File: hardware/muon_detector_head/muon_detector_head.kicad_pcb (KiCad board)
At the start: 2 copper layers, 60 x 75 mm, 22 parts, among them J1 Conn_01x08, U1 TPH2502, U2 TLV3502

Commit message: accepting updates
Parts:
- moved J1 11.4 mm to (7.55, 9.85)
- moved C6 2.55 mm to (32.0, 24.4)
- renumbered REF** to H1, REF** to H2, REF** to H3, REF** to H4
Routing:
- net VBIAS: track 33.3 -> 0.00 mm, vias 1 -> 0
- net GND: track 1.09 -> 0.00 mm, vias 1 -> 0
- net /SIPM_RAW: track 1.05 -> 0.00 mm
- added copper zone on B.Cu, net GND
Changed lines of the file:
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@@
 	)
 	(setup
+		(stackup
+			(layer "F.SilkS"
+				(type "Top Silk Screen")
+				(color "White")
+			)
+			(layer "F.Paste"
+				(type "Top Solder Paste")
+			)
+			(layer "F.Mask"
+				(type "Top Solder Mask")
+				(color "Green")
+				(thickness 0.01)
+			)
+			(layer "F.Cu"
+				(type "copper")
+				(thickness 0.035)
+			)
+			(layer "dielectric 1"
+				(type "core")
+				(thickness 1.51)
+				(material "FR4")
+				(epsilon_r 4.5)
+				(loss_tangent 0.02)
+			)
+			(layer "B.Cu"
+				(type "copper")
+				(thickness 0.035)
+			)
+			(layer "B.Mask"
+				(type "Bottom Solder Mask")
+				(color "Green")
+				(thickness 0.01)
+			)
+			(layer "B.Paste"
+				(type "Bottom Solder Paste")
+			)
+			(layer "B.SilkS"
+				(type "Bottom Silk Screen")
+				(color "White")
+			)
+			(copper_finish "None")
+			(dielectric_constraints no)
+		)
 		(pad_to_mask_clearance 0)
 		(allow_soldermask_bridges_in_footprints no)
@@
 		(descr "Mounting Hole 2.5mm, no annular, generated by kicad-footprint-generator mountinghole.py")
 		(tags "mountinghole")
-		(property "Reference" "REF**"
+		(property "Reference" "H1"
 			(at 0 -3.45 0)
 			(layer "F.SilkS")
+			(hide yes)
 			(effects
 				(font
@@
 			)
 		)
-		(attr exclude_from_pos_files exclude_from_bom)
+		(attr board_only exclude_from_pos_files exclude_from_bom)
 		(fp_circle
 			(center 0 0)
@@
 		(descr "Mounting Hole 2.5mm, no annular, generated by kicad-footprint-generator mountinghole.py")
 		(tags "mountinghole")
-		(property "Reference" "REF**"
+		(property "Reference" "H2"
 			(at 0 -3.45 0)
 			(layer "F.SilkS")
+			(hide yes)
 			(effects
 				(font
@@
 			)
 		)
-		(attr exclude_from_pos_files exclude_from_bom)
+		(attr board_only exclude_from_pos_files exclude_from_bom)
 		(fp_circle
 			(center 0 0)
@@
 		(descr "Mounting Hole 2.5mm, no annular, generated by kicad-footprint-generator mountinghole.py")
 		(tags "mountinghole")
-		(property "Reference" "REF**"
+		(property "Reference" "H3"
 			(at 0 -3.45 0)
 			(layer "F.SilkS")
+			(hide yes)
 			(effects
 				(font
@@
 			)
 		)
-		(attr exclude_from_pos_files exclude_from_bom)
+		(attr board_only exclude_from_pos_files exclude_from_bom)
 		(fp_circle
 			(center 0 0)
@@
 		(descr "Mounting Hole 2.5mm, no annular, generated by kicad-footprint-generator mountinghole.py")
 		(tags "mountinghole")
-		(property "Reference" "REF**"
+		(property "Reference" "H4"
 			(at 0 -3.45 0)
 			(layer "F.SilkS")
+			(hide yes)
 			(effects
 				(font
@@
 			)
 		)
-		(attr exclude_from_pos_files exclude_from_bom)
+		(attr board_only exclude_from_pos_files exclude_from_bom)
 		(fp_circle
 			(center 0 0)
@@
 	(footprint "Connector_PinHeader_2.54mm:PinHeader_1x08_P2.54mm_Vertical"
 		(layer "B.Cu")
-		(at 11.6 20.5 180)
+		(at 7.55 9.85 180)
 		(descr "Through hole straight pin header, 1x08, 2.54mm pitch, single row")
 		(tags "Through hole pin header THT 1x08 2.54mm single row")
@@
 	(footprint "Capacitor_SMD:C_0805_2012Metric"
 		(layer "B.Cu")
-		(at 32 27 180)
+		(at 32 24.45 180)
 		(descr "Capacitor SMD 0805 (2012 Metric), square (rectangular) end terminal, IPC-7351 nominal, (Body size source: IPC-SM-782 page 76, https://www.pcb-3d.com/wordpress/wp-content/uploads/ipc-sm-782a_amendment_1_and_2.pdf, https://docs.google.com/spreadsheets/d/1BsfQQcO9C6DZCsRaXUlFlo91Tg2WpOkGARC1WS5S8t0/edit?usp=sharing), generated with kicad-footprint-generator")
 		(tags "capacitor")
@@
 	)
 	(segment
-		(start 27 27.15)
-		(end 27 28.2)
-		(width 0.5)
-		(layer "F.Cu")
-		(net 2)
-	)
-	(via
-		(at 20.4875 35)
-		(size 0.6)
-		(drill 0.3)
-		(layers "F.Cu" "B.Cu")
-		(net 3)
-	)
-	(segment
-		(start 21.575 35)
-		(end 20.4875 35)
-		(width 0.5)
-		(layer "B.Cu")
-		(net 3)
-	)
-	(segment
-		(start 33 32.85)
-		(end 34.65 32.85)
-		(width 0.5)
-		(layer "F.Cu")
-		(net 7)
-	)
-	(segment
-		(start 34.65 32.85)
-		(end 34.7 32.8)
-		(width 0.5)
-		(layer "F.Cu")
-		(net 7)
-	)
-	(via
-		(at 34.7 32.8)
-		(size 0.6)
-		(drill 0.3)
-		(layers "F.Cu" "B.Cu")
-		(net 7)
-	)
-	(segment
-		(start 34.7 32.8)
-		(end 34.7 27)
-		(width 0.5)
-		(layer "B.Cu")
-		(net 7)
-	)
-	(segment
-		(start 32.95 27)
-		(end 26.45 20.5)
-		(width 0.5)
-		(layer "B.Cu")
-		(net 7)
-	)
-	(segment
-		(start 26.45 20.5)
-		(end 11.6 20.5)
-		(width 0.5)
-		(layer "B.Cu")
-		(net 7)
-	)
-	(segment
-		(start 34.7 27)
-		(end 32.95 27)
-		(width 0.5)
-		(layer "B.Cu")
-		(net 7)
-	)
-	(segment
 		(start 40.925 48.9875)
 		(end 40.9125 49)
-		(width 0.25)
+		(width 0.5)
 		(layer "B.Cu")
 		(net 9)
@@
 		(start 25.365 43.550001)
 		(end 25.365 44.525)
-		(width 0.25)
+		(width 0.5)
 		(layer "B.Cu")
 		(net 10)
@@
 		(start 34.85 60.75)
 		(end 36 60.75)
-		(width 0.25)
+		(width 0.5)
 		(layer "B.Cu")
 		(net 13)
@@
 			)
 		)
+	)
+	(zone
+		(net 3)
+		(net_name "GND")
+		(layer "B.Cu")
+		(hatch edge 0.5)
+		(connect_pads
+			(clearance 0.4)
+		)
+		(min_thickness 0.4)
+		(filled_areas_thickness no)
+		(fill yes
+			(thermal_gap 0.4)
+			(thermal_bridge_width 0.5)
+		)
+		(polygon
+			(pts
+				(xy 1 1) (xy 59 1) (xy 59 74) (xy 1 74)
+			)
+		)

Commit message: autorouting bad
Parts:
- C1, C2, C3, C4, C5, C6, J1, R1, R2, R3, R4, R5, R6, R7, RV1, U1, U2: moved to F.Cu
- D1: moved to B.Cu
- moved J1 49.0 mm to (56.5, 11.8), turned to 0 degrees
- moved C5 48.3 mm to (49.4, 23.4), turned to -90 degrees
- moved C4 47.3 mm to (52.3, 23.4), turned to -90 degrees
- moved C3 45.0 mm to (49.0, 18.6), turned to -90 degrees
- moved C2 44.9 mm to (51.6, 18.5), turned to -90 degrees
- moved R7 40.7 mm to (52.3, 33.0), turned to 0 degrees
- moved U2 30.5 mm to (50.8, 40.3), turned to 180 degrees
- moved R5 27.4 mm to (44.4, 31.7)
- moved R6 26.4 mm to (45.2, 38.6), turned to -90 degrees
- moved R1 21.7 mm to (40.6, 23.1), turned to 90 degrees
- moved C1 18.5 mm to (39.8, 26.7), turned to 180 degrees
- moved RV1 17.3 mm to (51.1, 49.5), turned to 90 degrees
- moved U1 16.7 mm to (40.0, 37.9)
- moved C6 15.4 mm to (28.0, 39.4), turned to 0 degrees
- moved R2 12.7 mm to (39.7, 29.2)
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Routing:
- net +3.3V: track 0.00 -> 113.7 mm
- net VBIAS: track 0.00 -> 90.9 mm
- net +5V: track 0.00 -> 65.5 mm, vias 0 -> 1
- net GND: track 0.00 -> 60.1 mm, vias 0 -> 3
- net /VBASE: track 0.00 -> 41.6 mm, vias 0 -> 2
- net /VBASE_DIV: track 0.02 -> 30.8 mm
- net /AMP_OUT: track 0.00 -> 16.6 mm
- net /SIPM_RAW: track 0.00 -> 12.5 mm, vias 0 -> 1
- net Net-(R7-Pad2): track 0.00 -> 11.0 mm
- net Net-(U1A--): track 0.97 -> 10.9 mm
- net /VTH: track 1.15 -> 10.8 mm
- net /AMP_IN: track 0.05 -> 9.00 mm
- net /TRIG: track 0.00 -> 8.11 mm

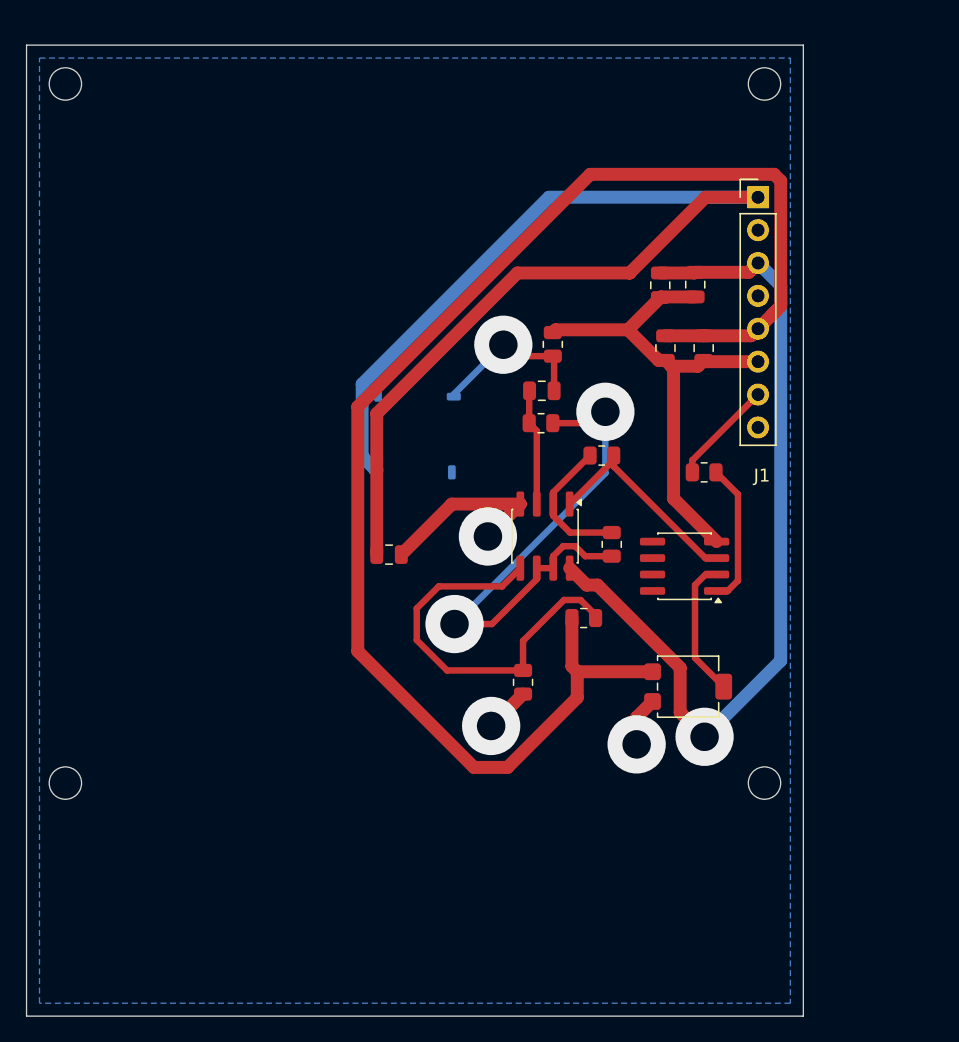
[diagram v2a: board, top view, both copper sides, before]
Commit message: feat: update detector head to include adc
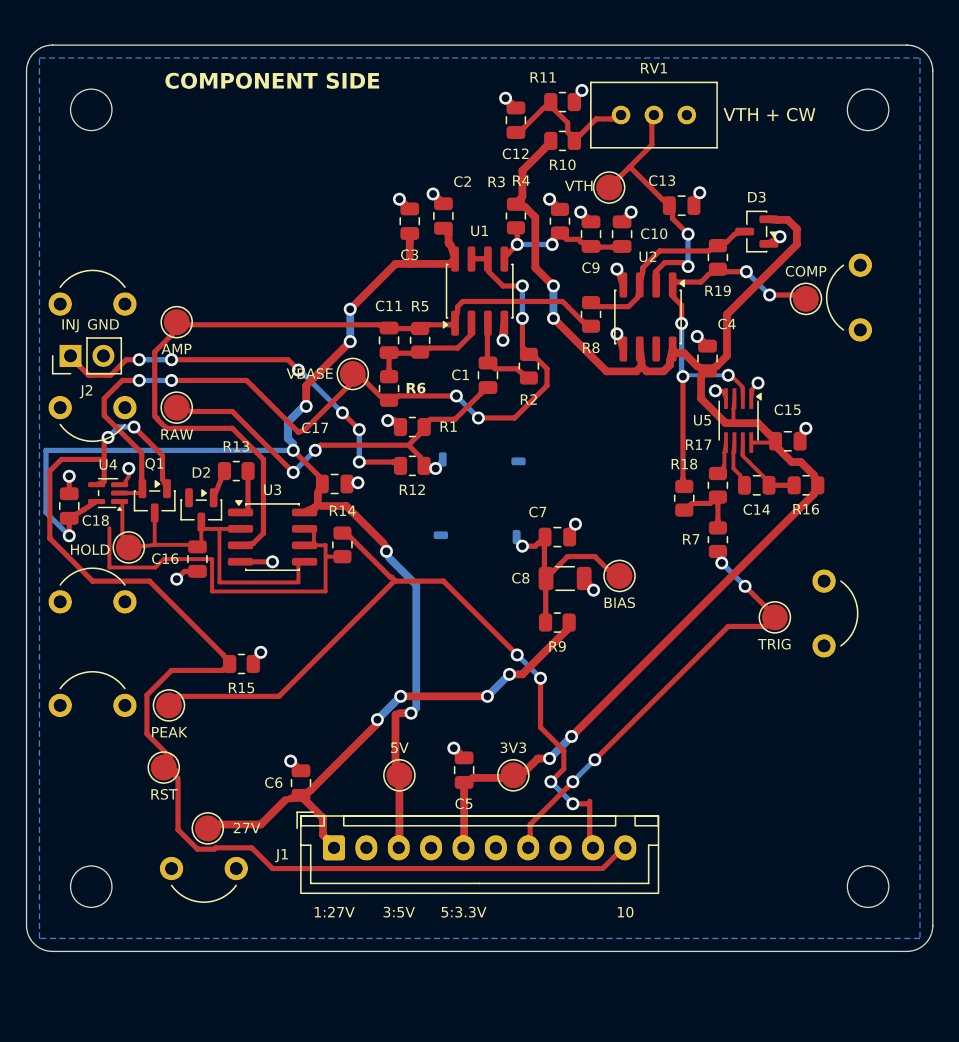
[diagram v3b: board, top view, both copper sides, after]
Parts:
- added C10: 100n, Capacitor_SMD:C_0805_2012Metric, F.Cu at (46.0, 14.6)
- added C11: 2.2p C0G, Capacitor_SMD:C_0805_2012Metric, F.Cu at (28.0, 22.8)
- added C12: 1u, Capacitor_SMD:C_0805_2012Metric, F.Cu at (37.8, 5.80)
- added C13: 10n 100V C0G, Capacitor_SMD:C_0805_2012Metric, F.Cu at (50.6, 12.4)
- added C14: 27p C0G, Capacitor_SMD:C_0805_2012Metric, F.Cu at (56.4, 34.0)
- added C15: 100n, Capacitor_SMD:C_0805_2012Metric, F.Cu at (58.8, 30.6)
- added C16: 220p C0G, Capacitor_SMD:C_0805_2012Metric, F.Cu at (13.2, 39.7)
- added C17: 100n, Capacitor_SMD:C_0805_2012Metric, F.Cu at (23.8, 33.9)
- added C18: 100n, Capacitor_SMD:C_0805_2012Metric, F.Cu at (3.30, 35.6)
- added C7: 10n 100V C0G, Capacitor_SMD:C_0805_2012Metric, F.Cu at (41.0, 38.0)
- added C8: 1u 50V, Capacitor_SMD:C_1206_3216Metric, F.Cu at (41.6, 41.2)
- added C9: 1u, Capacitor_SMD:C_0805_2012Metric, F.Cu at (43.6, 14.6)
- added D2: BAS70, Package_TO_SOT_SMD:SOT-23, F.Cu at (13.5, 35.9)
- added D3: BAT54S, Package_TO_SOT_SMD:SOT-23, F.Cu at (56.4, 14.4)
- added J2: INJECT, Connector_PinHeader_2.54mm:PinHeader_1x02_P2.54mm_Vertical, F.Cu at (3.40, 24.0)
- added Q1: BSS138P, Package_TO_SOT_SMD:SOT-23, F.Cu at (9.90, 35.2)
- added R10: 4.70k, Resistor_SMD:R_0805_2012Metric, F.Cu at (41.4, 7.40)
- added R11: 1.00k, Resistor_SMD:R_0805_2012Metric, F.Cu at (41.4, 4.40)
- added R12: 499, Resistor_SMD:R_0805_2012Metric, F.Cu at (29.8, 32.5)
- added R13: 82.0, Resistor_SMD:R_0805_2012Metric, F.Cu at (16.2, 32.9)
- added R14: 100, Resistor_SMD:R_0805_2012Metric, F.Cu at (24.4, 38.6)
- added R15: 100k, Resistor_SMD:R_0805_2012Metric, F.Cu at (16.6, 47.8)
- added R16: 2.00k, Resistor_SMD:R_0805_2012Metric, F.Cu at (60.2, 34.0)
- added R17: 0, Resistor_SMD:R_0805_2012Metric, F.Cu at (53.4, 34.0)
- added R18: 0, Resistor_SMD:R_0805_2012Metric, F.Cu at (50.8, 35.0)
- added R19: 330k, Resistor_SMD:R_0805_2012Metric, F.Cu at (53.4, 16.4)
- added R8: 1.00k, Resistor_SMD:R_0805_2012Metric, F.Cu at (43.6, 20.8)
- added R9: 100, Resistor_SMD:R_0805_2012Metric, F.Cu at (41.0, 44.6)
- added TP1: VBIAS, TestPoint:TestPoint_Pad_D2.0mm, F.Cu at (14.0, 60.5)
- added TP10: TRIG, TestPoint:TestPoint_Pad_D2.0mm, F.Cu at (57.8, 44.2)
- added TP11: PEAK_HOLD, TestPoint:TestPoint_Pad_D2.0mm, F.Cu at (7.90, 38.8)
- added TP12: PEAK_OUT, TestPoint:TestPoint_Pad_D2.0mm, F.Cu at (11.0, 51.0)
- added TP13: PEAK_RESET, TestPoint:TestPoint_Pad_D2.0mm, F.Cu at (10.6, 55.8)
- added TP14: GND_LOOP, MuonTelescopeParts:TestPoint_GroundLoop_P5.00mm_Drill1.0mm, F.Cu at (16.2, 63.6)
- added TP15: GND_LOOP, MuonTelescopeParts:TestPoint_GroundLoop_P5.00mm_Drill1.0mm, F.Cu at (7.60, 28.0)
- added TP16: GND_LOOP, MuonTelescopeParts:TestPoint_GroundLoop_P5.00mm_Drill1.0mm, F.Cu at (2.60, 20.0)
- added TP17: GND_LOOP, MuonTelescopeParts:TestPoint_GroundLoop_P5.00mm_Drill1.0mm, F.Cu at (64.4, 22.0)
- added TP18: GND_LOOP, MuonTelescopeParts:TestPoint_GroundLoop_P5.00mm_Drill1.0mm, F.Cu at (61.6, 41.4)
- added TP19: GND_LOOP, MuonTelescopeParts:TestPoint_GroundLoop_P5.00mm_Drill1.0mm, F.Cu at (2.60, 43.0)
- added TP2: BIAS_LOCAL, TestPoint:TestPoint_Pad_D2.0mm, F.Cu at (45.8, 41.0)
- added TP20: GND_LOOP, MuonTelescopeParts:TestPoint_GroundLoop_P5.00mm_Drill1.0mm, F.Cu at (2.60, 51.0)
- added TP3: +5V, TestPoint:TestPoint_Pad_D2.0mm, F.Cu at (28.8, 56.4)
- added TP4: +3.3V, TestPoint:TestPoint_Pad_D2.0mm, F.Cu at (37.6, 56.4)
- added TP5: VBASE, TestPoint:TestPoint_Pad_D2.0mm, F.Cu at (25.2, 25.4)
- added TP6: SIPM_RAW, TestPoint:TestPoint_Pad_D2.0mm, F.Cu at (11.6, 28.0)
- added TP7: AMP_OUT, TestPoint:TestPoint_Pad_D2.0mm, F.Cu at (11.6, 21.4)
- added TP8: VTH, TestPoint:TestPoint_Pad_D2.0mm, F.Cu at (45.0, 11.0)
- added TP9: COMP_RAW, TestPoint:TestPoint_Pad_D2.0mm, F.Cu at (60.2, 19.6)
- added U3: TPH2502, Package_SO:SOIC-8_3.9x4.9mm_P1.27mm, F.Cu at (19.0, 38.0)
- added U4: TMUX1101, Package_TO_SOT_SMD:SOT-353_SC-70-5, F.Cu at (6.30, 34.6)
- added U5: SN74LVC1G123, Package_SO:SSOP-8_2.95x2.8mm_P0.65mm, F.Cu at (55.0, 29.0)
- C3: value 10u -> 4.7u
- H1, H2, H3, H4: value MountingHole_2.5mm -> MountingHole_3.2mm; footprint MountingHole:MountingHole_2.5mm -> MuonTelescopeParts:MountingHole_3.2mm
- J1: value Conn_01x08 -> B10B-XH-A; footprint Connector_PinHeader_2.54mm:PinHeader_1x08_P2.54mm_Vertical -> Connector_JST:JST_XH_B10B-XH-A_1x10_P2.50mm_Vertical
- RV1: footprint Potentiometer_SMD:Potentiometer_Bourns_3314G_Vertical -> Potentiometer_THT:Potentiometer_Bourns_3296W_Vertical
- moved J1 60.0 mm to (23.8, 62.0)
- moved RV1 44.2 mm to (51.0, 5.40), turned to 0 degrees
- moved C5 36.1 mm to (33.8, 56.0), turned to 90 degrees
- moved R4 35.7 mm to (41.2, 13.6), turned to 90 degrees
- moved R3 31.5 mm to (37.8, 13.2), turned to -90 degrees
- moved R6 21.0 mm to (28.0, 26.5)
- moved C2 20.2 mm to (32.2, 13.2), turned to 90 degrees
- moved C3 20.0 mm to (29.6, 13.6), turned to 90 degrees
- moved U1 19.6 mm to (35.0, 19.0), turned to 90 degrees
- moved U2 19.5 mm to (48.0, 21.0), turned to -90 degrees
- moved C6 18.9 mm to (21.2, 57.0), turned to 90 degrees
- moved R5 16.6 mm to (30.4, 22.8), turned to -90 degrees
- moved R1 12.6 mm to (29.8, 29.5), turned to 180 degrees
- moved H3 11.3 mm to (65.0, 65.0)
- moved H2 8.25 mm to (65.0, 5.00)
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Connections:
- net Net-(U1A--) renamed /AMP_FB
- D1 pad 3: VBIAS -> /BIAS_LOCAL
- D1 pad 4: unconnected-(D1-NC-Pad4) -> GND
- R7 pad 1: /TRIG -> Net-(R17-Pad2)
- R7 pad 2: Net-(R7-Pad2) -> /TRIG
- RV1 pad 1: +3.3V -> GND
- RV1 pad 3: GND -> Net-(C12-Pad1)
- U2 pad 1: Net-(R7-Pad2) -> /COMP_RAW
- U2 pad 3: /AMP_OUT -> /COMP_IN
- U2 pad 5: unconnected-(U2B-+-Pad5) -> GND
- U2 pad 6: unconnected-(U2B---Pad6) -> +3.3V
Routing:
- net /PEAK_RESET: track 0.00 -> 95.4 mm, vias 0 -> 2
- net /PEAK_OUT: track 0.00 -> 57.6 mm, vias 0 -> 4
- net VBIAS: track 90.9 -> 39.3 mm, vias 0 -> 4
- net /AMP_OUT: track 16.6 -> 59.5 mm
- net /COMP_RAW: track 0.00 -> 33.3 mm, vias 0 -> 5
- net /INJECT: track 0.00 -> 31.4 mm, vias 0 -> 6
- net /PEAK_GUARD: track 0.00 -> 29.5 mm
- net +5V: track 65.5 -> 94.1 mm, vias 1 -> 7
- net GND: track 60.1 -> 33.2 mm, vias 3 -> 27
- net /TRIG: track 8.11 -> 34.2 mm, vias 0 -> 4
- net /PEAK_HOLD: track 0.00 -> 26.0 mm
- net /VBASE: track 41.6 -> 64.9 mm, vias 2 -> 6
- net /SIPM_RAW: track 12.5 -> 32.3 mm, vias 1 -> 3
- net /VBASE_DIV: track 30.8 -> 11.8 mm, vias 0 -> 2
- net /BIAS_LOCAL: track 0.00 -> 16.4 mm, vias 0 -> 1
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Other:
- board size 60 x 75 mm -> 70 x 70 mm
- board text added: "10"
- board text added: "1:27V"
- board text added: "27V"
- board text added: "3:5V"
- board text added: "3V3"
- board text added: "5:3.3V"
- board text added: "5V"
- board text added: "AMP"
- board text added: "BIAS"
- board text added: "COMP"
- board text added: "COMPONENT SIDE"
- board text added: "GND"
- board text added: "HOLD"
- board text added: "INJ"
- board text added: "OPTICAL SIDE"
- board text added: "PEAK"
- board text added: "RAW"
- board text added: "RST"
- board text added: "TRIG"
- board text added: "VBASE"
- board text added: "VTH"
- board text added: "VTH + CW"
